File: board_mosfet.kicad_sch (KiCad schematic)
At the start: 14 parts, among them J2 USB_IN, J3 USB_OUT, J5 USB_OUT, Q1 Q_NMOS_GDS, Q2 Q_NMOS_GDS, U1 AMS1117-3.3, U2 INA219AxD, U3 INA219AxD

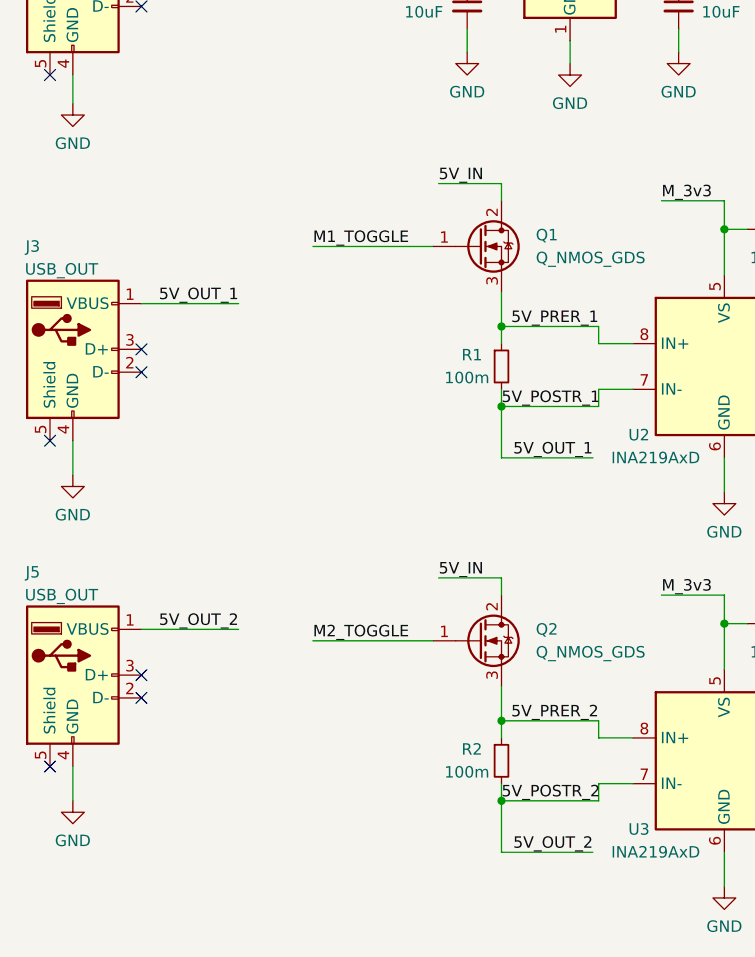
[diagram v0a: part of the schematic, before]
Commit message: Fixed error with mosfet arrangement.
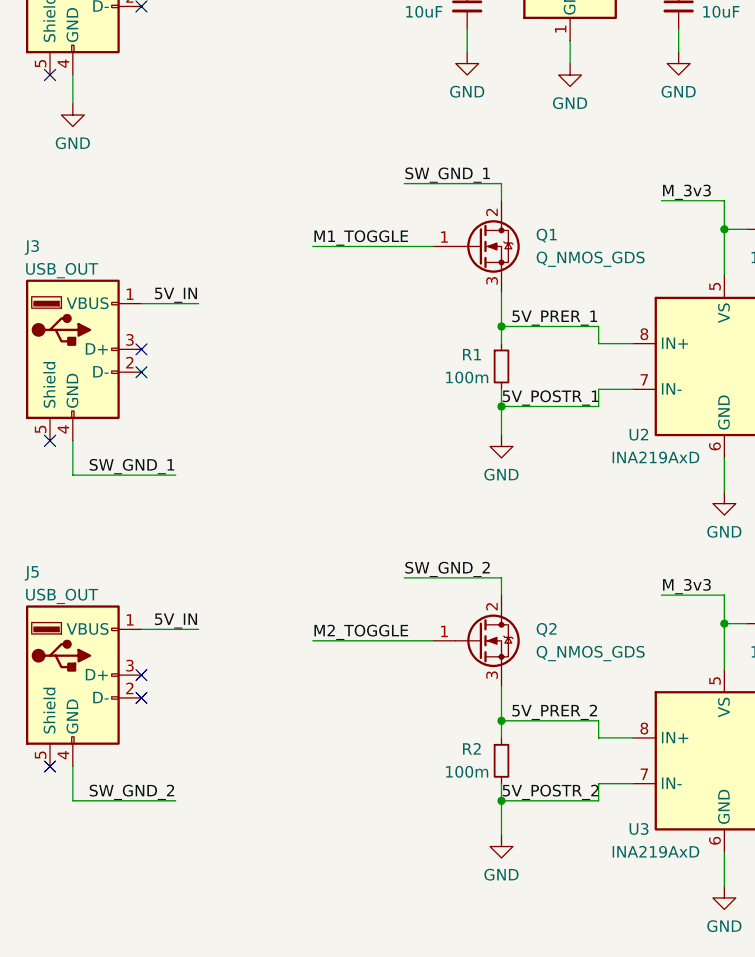
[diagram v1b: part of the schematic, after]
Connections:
- net 5V_IN: now also J3.1 (VBUS), J5.1 (VBUS); no longer Q1.2 (D), Q2.2 (D)
- net GND: now also R1.2, R2.2, U2.7 (IN-), U3.7 (IN-); no longer J3.4 (GND), J5.4 (GND)
- removed net 5V_OUT_1: J3.1 (VBUS), R1.2, U2.7 (IN-)
- removed net 5V_OUT_2: J5.1 (VBUS), R2.2, U3.7 (IN-)
- new net SW_GND_1: J3.4 (GND), Q1.2 (D)
- new net SW_GND_2: J5.4 (GND), Q2.2 (D)
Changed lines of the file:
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@@
     (stroke (width 0) (type default) (color 0 0 0 0))
   )
-  (wire (pts (xy 85.09 135.89) (xy 85.09 141.605))
+  (wire (pts (xy 85.09 135.89) (xy 85.09 139.7))
     (stroke (width 0) (type default) (color 0 0 0 0))
   )
@@
     (stroke (width 0) (type default) (color 0 0 0 0))
   )
+  (wire (pts (xy 37.465 99.695) (xy 48.895 99.695))
+    (stroke (width 0) (type default) (color 0 0 0 0))
+  )
   (wire (pts (xy 109.855 116.205) (xy 112.395 116.205))
     (stroke (width 0) (type default) (color 0 0 0 0))
@@
     (stroke (width 0) (type default) (color 0 0 0 0))
   )
-  (wire (pts (xy 85.09 92.075) (xy 85.09 97.79))
-    (stroke (width 0) (type default) (color 0 0 0 0))
-  )
-  (wire (pts (xy 78.105 111.125) (xy 85.09 111.125))
-    (stroke (width 0) (type default) (color 0 0 0 0))
-  )
-  (wire (pts (xy 95.25 141.605) (xy 85.09 141.605))
+  (wire (pts (xy 85.09 92.075) (xy 85.09 95.25))
+    (stroke (width 0) (type default) (color 0 0 0 0))
+  )
+  (wire (pts (xy 74.295 111.125) (xy 85.09 111.125))
     (stroke (width 0) (type default) (color 0 0 0 0))
   )
@@
     (stroke (width 0) (type default) (color 0 0 0 0))
   )
-  (wire (pts (xy 95.25 97.79) (xy 85.09 97.79))
-    (stroke (width 0) (type default) (color 0 0 0 0))
-  )
   (wire (pts (xy 109.855 72.39) (xy 112.395 72.39))
     (stroke (width 0) (type default) (color 0 0 0 0))
@@
     (stroke (width 0) (type default) (color 0 0 0 0))
   )
-  (wire (pts (xy 45.085 80.645) (xy 55.88 80.645))
+  (wire (pts (xy 45.085 80.645) (xy 51.435 80.645))
     (stroke (width 0) (type default) (color 0 0 0 0))
   )
@@
     (stroke (width 0) (type default) (color 0 0 0 0))
   )
+  (wire (pts (xy 37.465 135.89) (xy 48.895 135.89))
+    (stroke (width 0) (type default) (color 0 0 0 0))
+  )
   (wire (pts (xy 109.855 113.03) (xy 109.855 116.205))
     (stroke (width 0) (type default) (color 0 0 0 0))
   )
-  (wire (pts (xy 45.085 116.84) (xy 55.88 116.84))
+  (wire (pts (xy 45.085 116.84) (xy 51.435 116.84))
     (stroke (width 0) (type default) (color 0 0 0 0))
   )
@@
     (stroke (width 0) (type default) (color 0 0 0 0))
   )
-  (wire (pts (xy 78.105 67.31) (xy 85.09 67.31))
+  (wire (pts (xy 74.295 67.31) (xy 85.09 67.31))
     (stroke (width 0) (type default) (color 0 0 0 0))
   )
@@
     (effects (font (size 1.27 1.27)) (justify left bottom))
   )
-  (label "5V_IN" (at 78.105 67.31 0)
-    (effects (font (size 1.27 1.27)) (justify left bottom))
-  )
   (label "M1_TOGGLE" (at 64.135 74.295 0)
     (effects (font (size 1.27 1.27)) (justify left bottom))
@@
     (effects (font (size 1.27 1.27)) (justify left bottom))
   )
+  (label "5V_IN" (at 51.435 80.645 180)
+    (effects (font (size 1.27 1.27)) (justify right bottom))
+  )
   (label "M_I2C_SDA" (at 186.69 37.465 180)
     (effects (font (size 1.27 1.27)) (justify right bottom))
@@
     (effects (font (size 1.27 1.27)) (justify right bottom))
   )
-  (label "5V_OUT_2" (at 55.88 116.84 180)
-    (effects (font (size 1.27 1.27)) (justify right bottom))
-  )
   (label "M2_TOGGLE" (at 186.69 47.625 180)
     (effects (font (size 1.27 1.27)) (justify right bottom))
@@
     (effects (font (size 1.27 1.27)) (justify left bottom))
   )
-  (label "5V_OUT_2" (at 95.25 141.605 180)
-    (effects (font (size 1.27 1.27)) (justify right bottom))
-  )
   (label "5V_PRER_1" (at 95.885 83.185 180)
     (effects (font (size 1.27 1.27)) (justify right bottom))
   )
-  (label "5V_OUT_1" (at 95.25 97.79 180)
-    (effects (font (size 1.27 1.27)) (justify right bottom))
-  )
   (label "5V_IN" (at 71.12 43.815 0)
     (effects (font (size 1.27 1.27)) (justify left bottom))
   )
-  (label "5V_OUT_1" (at 55.88 80.645 180)
-    (effects (font (size 1.27 1.27)) (justify right bottom))
-  )
   (label "M_I2C_SDA" (at 131.445 82.55 180)
     (effects (font (size 1.27 1.27)) (justify right bottom))
@@
     (effects (font (size 1.27 1.27)) (justify left bottom))
   )
+  (label "SW_GND_1" (at 48.895 99.695 180)
+    (effects (font (size 1.27 1.27)) (justify right bottom))
+  )
   (label "M_I2C_SCL" (at 186.69 42.545 180)
     (effects (font (size 1.27 1.27)) (justify right bottom))
   )
-  (label "5V_IN" (at 78.105 111.125 0)
+  (label "SW_GND_2" (at 74.295 111.125 0)
+    (effects (font (size 1.27 1.27)) (justify left bottom))
+  )
+  (label "5V_IN" (at 51.435 116.84 180)
+    (effects (font (size 1.27 1.27)) (justify right bottom))
+  )
+  (label "SW_GND_2" (at 48.895 135.89 180)
+    (effects (font (size 1.27 1.27)) (justify right bottom))
+  )
+  (label "SW_GND_1" (at 74.295 67.31 0)
     (effects (font (size 1.27 1.27)) (justify left bottom))
   )
@@
     (pin "1")
     (pin "2")
-  )
-  (symbol (lib_id "power:GND") (at 37.465 135.89 0) (unit 1)
-    (in_bom yes) (on_board yes) (fields_autoplaced)
-    (property "Reference" "#PWR018" (id 0) (at 37.465 142.24 0)
-      (effects (font (size 1.27 1.27)) hide)
-    )
-    (property "Value" "GND" (id 1) (at 37.465 140.335 0))
-    (property "Footprint" "" (id 2) (at 37.465 135.89 0)
-      (effects (font (size 1.27 1.27)) hide)
-    )
-    (property "Datasheet" "" (id 3) (at 37.465 135.89 0)
-      (effects (font (size 1.27 1.27)) hide)
-    )
-    (pin "1")
   )
   (symbol (lib_id "power:GND") (at 124.46 72.39 0) (unit 1)
@@
     (pin "4")
     (pin "5")
+  )
+  (symbol (lib_id "power:GND") (at 85.09 139.7 0) (unit 1)
+    (in_bom yes) (on_board yes) (fields_autoplaced)
+    (property "Reference" "#PWR?" (id 0) (at 85.09 146.05 0)
+      (effects (font (size 1.27 1.27)) hide)
+    )
+    (property "Value" "GND" (id 1) (at 85.09 144.145 0))
+    (property "Footprint" "" (id 2) (at 85.09 139.7 0)
+      (effects (font (size 1.27 1.27)) hide)
+    )
+    (property "Datasheet" "" (id 3) (at 85.09 139.7 0)
+      (effects (font (size 1.27 1.27)) hide)
+    )
+    (pin "1")
   )
   (symbol (lib_id "Analog_ADC:INA219AxD") (at 109.855 131.445 0) (unit 1)
@@
     (pin "3")
   )
-  (symbol (lib_id "power:GND") (at 37.465 99.695 0) (unit 1)
-    (in_bom yes) (on_board yes) (fields_autoplaced)
-    (property "Reference" "#PWR02" (id 0) (at 37.465 106.045 0)
-      (effects (font (size 1.27 1.27)) hide)
-    )
-    (property "Value" "GND" (id 1) (at 37.465 104.14 0))
-    (property "Footprint" "" (id 2) (at 37.465 99.695 0)
-      (effects (font (size 1.27 1.27)) hide)
-    )
-    (property "Datasheet" "" (id 3) (at 37.465 99.695 0)
-      (effects (font (size 1.27 1.27)) hide)
-    )
-    (pin "1")
-  )
   (symbol (lib_id "Connector:USB_A") (at 37.465 45.085 0) (unit 1)
     (in_bom yes) (on_board yes)
@@
     (pin "2")
   )
+  (symbol (lib_id "power:GND") (at 85.09 95.25 0) (unit 1)
+    (in_bom yes) (on_board yes) (fields_autoplaced)
+    (property "Reference" "#PWR?" (id 0) (at 85.09 101.6 0)
+      (effects (font (size 1.27 1.27)) hide)
+    )
+    (property "Value" "GND" (id 1) (at 85.09 99.695 0))
+    (property "Footprint" "" (id 2) (at 85.09 95.25 0)
+      (effects (font (size 1.27 1.27)) hide)
+    )
+    (property "Datasheet" "" (id 3) (at 85.09 95.25 0)
+      (effects (font (size 1.27 1.27)) hide)
+    )
+    (pin "1")
+  )
   (symbol (lib_id "power:GND") (at 201.295 48.26 0) (unit 1)

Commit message: Updated to v0.2.0
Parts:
- removed C1, C2: 100nF, Capacitor_SMD:C_0603_1608Metric, symbol Device:C_Small
- removed J3, J5: USB_OUT, Library:904-131A2032S10100, symbol Connector:USB_A
- removed Q1, Q2: Q_NMOS_GDS, Library:YJL3400A, symbol Device:Q_NMOS_GDS
- removed R1, R2: 100m, Resistor_SMD:R_2010_5025Metric, symbol Device:R_Small
- removed U2, U3: INA219AxD, Package_SO:SOIC-8_3.9x4.9mm_P1.27mm, symbol Analog_ADC:INA219AxD
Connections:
- no-connect marks 9 -> 3
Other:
- added sheet Switch Circuit (switch_circuit.kicad_sch)
- added sheet Switch Circuit1 (switch_circuit.kicad_sch)
- note added: "I2C Addr = 0x40"
- note added: "I2C Addr = 0x41"
- note removed: "I2C Addr: 0x40"
- note removed: "I2C Addr: 0x41"

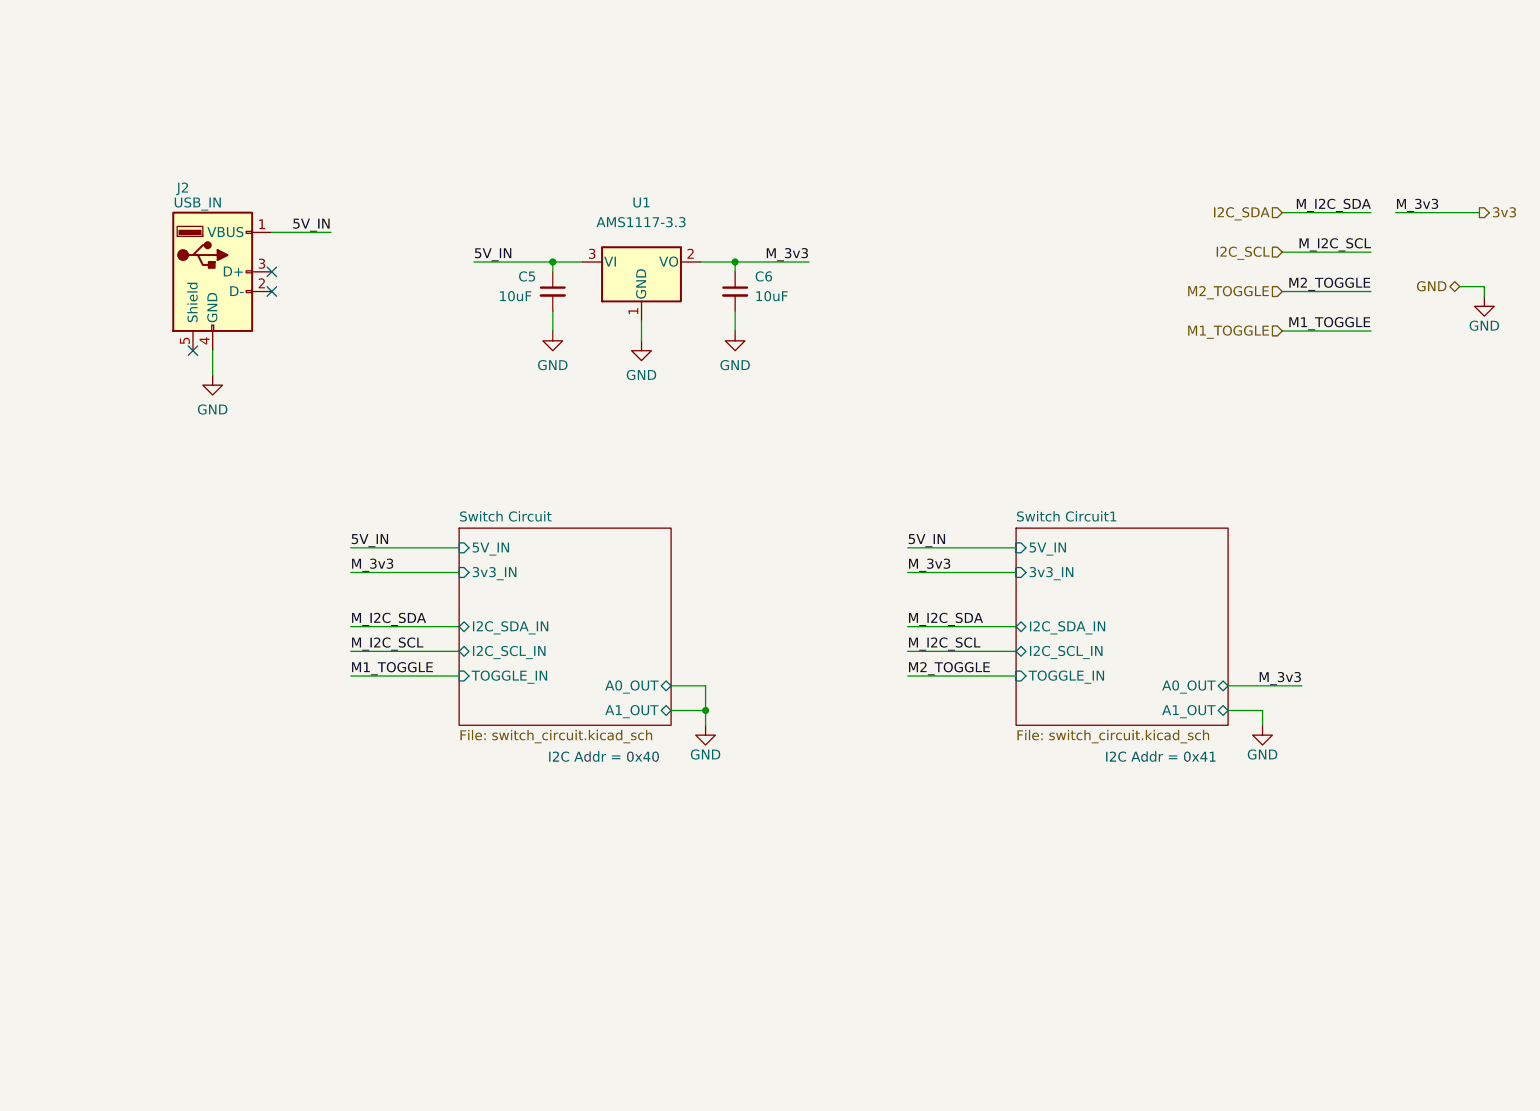
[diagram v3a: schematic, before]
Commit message: Made schematics pretty, added photos, added README
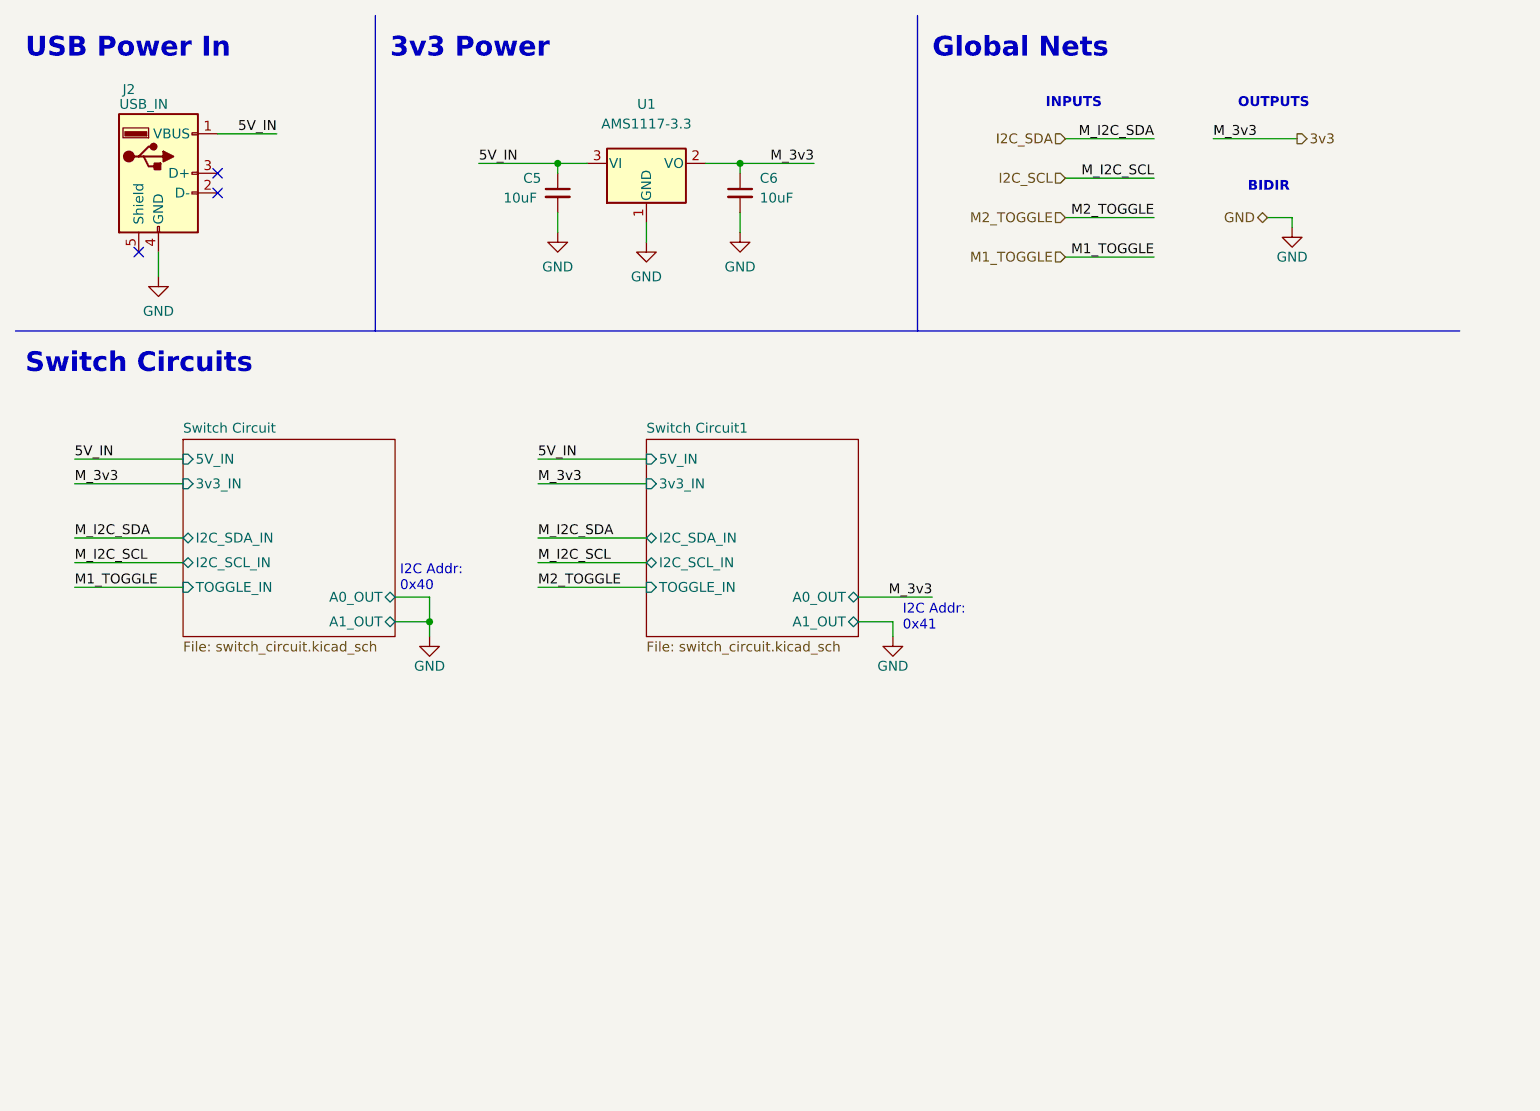
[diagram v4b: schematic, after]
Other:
- note added: "3v3 Power"
- note added: "BIDIR"
- note added: "Global Nets"
- note added: "I2C Addr: 0x40"
- note added: "I2C Addr: 0x41"
- note added: "INPUTS"
- note added: "OUTPUTS"
- note added: "Switch Circuits"
- note added: "USB Power In"
- note removed: "I2C Addr = 0x40"
- note removed: "I2C Addr = 0x41"
- title: Smart USB Port -> Wifi USB Port
- moved on the sheet: C5, C6, J2, U1
